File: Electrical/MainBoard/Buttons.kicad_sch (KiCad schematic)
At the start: 6 parts, among them SW10 User_Button, SW8 User_Button, SW9 User_Button

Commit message: Begin layout of pcb
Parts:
- renumbered SW9 to SW4, SW10 to SW5, SW8 to SW6
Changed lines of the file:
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@@
   (symbol (lib_id "power:+3.3V") (at 292.735 247.65 0) (unit 1)
     (in_bom yes) (on_board yes) (dnp no) (fields_autoplaced)
-    (property "Reference" "#PWR091" (at 292.735 251.46 0)
+    (property "Reference" "#PWR095" (at 292.735 251.46 0)
       (effects (font (size 1.27 1.27)) hide)
     )
@@
       (project "MainBoard"
         (path "/bd24c4db-4e36-4117-bd4f-5228ef241da9/41ea0116-63b8-412b-88a7-1e6a491b97c5"
-          (reference "#PWR091") (unit 1)
+          (reference "#PWR095") (unit 1)
         )
       )
@@
         )
         (path "/bd24c4db-4e36-4117-bd4f-5228ef241da9/41ea0116-63b8-412b-88a7-1e6a491b97c5"
-          (reference "R16") (unit 1)
+          (reference "R13") (unit 1)
         )
       )
@@
   (symbol (lib_id "power:+3.3V") (at 173.355 120.65 0) (unit 1)
     (in_bom yes) (on_board yes) (dnp no) (fields_autoplaced)
-    (property "Reference" "#PWR088" (at 173.355 124.46 0)
+    (property "Reference" "#PWR089" (at 173.355 124.46 0)
       (effects (font (size 1.27 1.27)) hide)
     )
@@
       (project "MainBoard"
         (path "/bd24c4db-4e36-4117-bd4f-5228ef241da9/41ea0116-63b8-412b-88a7-1e6a491b97c5"
-          (reference "#PWR088") (unit 1)
+          (reference "#PWR089") (unit 1)
         )
       )
@@
   (symbol (lib_id "Switch:SW_Push") (at 184.15 121.92 0) (unit 1)
     (in_bom yes) (on_board yes) (dnp no) (fields_autoplaced)
-    (property "Reference" "SW9" (at 184.15 114.3 0)
+    (property "Reference" "SW4" (at 184.15 114.3 0)
       (effects (font (size 1.27 1.27)))
     )
@@
       (project "MainBoard"
         (path "/bd24c4db-4e36-4117-bd4f-5228ef241da9/41ea0116-63b8-412b-88a7-1e6a491b97c5"
-          (reference "SW9") (unit 1)
+          (reference "SW4") (unit 1)
         )
       )
@@
   (symbol (lib_id "power:GND") (at 292.735 254.635 0) (unit 1)
     (in_bom yes) (on_board yes) (dnp no) (fields_autoplaced)
-    (property "Reference" "#PWR090" (at 292.735 260.985 0)
+    (property "Reference" "#PWR096" (at 292.735 260.985 0)
       (effects (font (size 1.27 1.27)) hide)
     )
@@
       (project "MainBoard"
         (path "/bd24c4db-4e36-4117-bd4f-5228ef241da9/41ea0116-63b8-412b-88a7-1e6a491b97c5"
-          (reference "#PWR090") (unit 1)
+          (reference "#PWR096") (unit 1)
         )
       )
@@
   (symbol (lib_id "power:GND") (at 192.405 129.54 0) (unit 1)
     (in_bom yes) (on_board yes) (dnp no) (fields_autoplaced)
-    (property "Reference" "#PWR085" (at 192.405 135.89 0)
+    (property "Reference" "#PWR092" (at 192.405 135.89 0)
       (effects (font (size 1.27 1.27)) hide)
     )
@@
       (project "MainBoard"
         (path "/bd24c4db-4e36-4117-bd4f-5228ef241da9/41ea0116-63b8-412b-88a7-1e6a491b97c5"
-          (reference "#PWR085") (unit 1)
+          (reference "#PWR092") (unit 1)
         )
       )
@@
   (symbol (lib_id "Switch:SW_Push") (at 184.785 100.33 0) (unit 1)
     (in_bom yes) (on_board yes) (dnp no) (fields_autoplaced)
-    (property "Reference" "SW8" (at 184.785 92.71 0)
+    (property "Reference" "SW6" (at 184.785 92.71 0)
       (effects (font (size 1.27 1.27)))
     )
@@
       (project "MainBoard"
         (path "/bd24c4db-4e36-4117-bd4f-5228ef241da9/41ea0116-63b8-412b-88a7-1e6a491b97c5"
-          (reference "SW8") (unit 1)
+          (reference "SW6") (unit 1)
         )
       )
@@
   (symbol (lib_id "power:+3.3V") (at 173.99 99.06 0) (unit 1)
     (in_bom yes) (on_board yes) (dnp no) (fields_autoplaced)
-    (property "Reference" "#PWR087" (at 173.99 102.87 0)
+    (property "Reference" "#PWR091" (at 173.99 102.87 0)
       (effects (font (size 1.27 1.27)) hide)
     )
@@
       (project "MainBoard"
         (path "/bd24c4db-4e36-4117-bd4f-5228ef241da9/41ea0116-63b8-412b-88a7-1e6a491b97c5"
-          (reference "#PWR087") (unit 1)
+          (reference "#PWR091") (unit 1)
         )
       )
@@
   (symbol (lib_id "power:GND") (at 192.405 147.955 0) (unit 1)
     (in_bom yes) (on_board yes) (dnp no) (fields_autoplaced)
-    (property "Reference" "#PWR086" (at 192.405 154.305 0)
+    (property "Reference" "#PWR093" (at 192.405 154.305 0)
       (effects (font (size 1.27 1.27)) hide)
     )
@@
       (project "MainBoard"
         (path "/bd24c4db-4e36-4117-bd4f-5228ef241da9/41ea0116-63b8-412b-88a7-1e6a491b97c5"
-          (reference "#PWR086") (unit 1)
+          (reference "#PWR093") (unit 1)
         )
       )
@@
   (symbol (lib_id "Switch:SW_Push") (at 184.15 140.335 0) (unit 1)
     (in_bom yes) (on_board yes) (dnp no) (fields_autoplaced)
-    (property "Reference" "SW10" (at 184.15 132.715 0)
+    (property "Reference" "SW5" (at 184.15 132.715 0)
       (effects (font (size 1.27 1.27)))
     )
@@
       (project "MainBoard"
         (path "/bd24c4db-4e36-4117-bd4f-5228ef241da9/41ea0116-63b8-412b-88a7-1e6a491b97c5"
-          (reference "SW10") (unit 1)
+          (reference "SW5") (unit 1)
         )
       )
@@
         )
         (path "/bd24c4db-4e36-4117-bd4f-5228ef241da9/41ea0116-63b8-412b-88a7-1e6a491b97c5"
-          (reference "R15") (unit 1)
+          (reference "R12") (unit 1)
         )
       )
@@
   (symbol (lib_id "power:+3.3V") (at 173.355 139.065 0) (unit 1)
     (in_bom yes) (on_board yes) (dnp no) (fields_autoplaced)
-    (property "Reference" "#PWR089" (at 173.355 142.875 0)
+    (property "Reference" "#PWR090" (at 173.355 142.875 0)
       (effects (font (size 1.27 1.27)) hide)
     )
@@
       (project "MainBoard"
         (path "/bd24c4db-4e36-4117-bd4f-5228ef241da9/41ea0116-63b8-412b-88a7-1e6a491b97c5"
-          (reference "#PWR089") (unit 1)
+          (reference "#PWR090") (unit 1)
         )
       )
@@
   (symbol (lib_id "power:GND") (at 193.04 107.95 0) (unit 1)
     (in_bom yes) (on_board yes) (dnp no) (fields_autoplaced)
-    (property "Reference" "#PWR084" (at 193.04 114.3 0)
+    (property "Reference" "#PWR094" (at 193.04 114.3 0)
       (effects (font (size 1.27 1.27)) hide)
     )
@@
       (project "MainBoard"
         (path "/bd24c4db-4e36-4117-bd4f-5228ef241da9/41ea0116-63b8-412b-88a7-1e6a491b97c5"
-          (reference "#PWR084") (unit 1)
-        )
-      )
+          (reference "#PWR094") (unit 1)
+        )
+      )

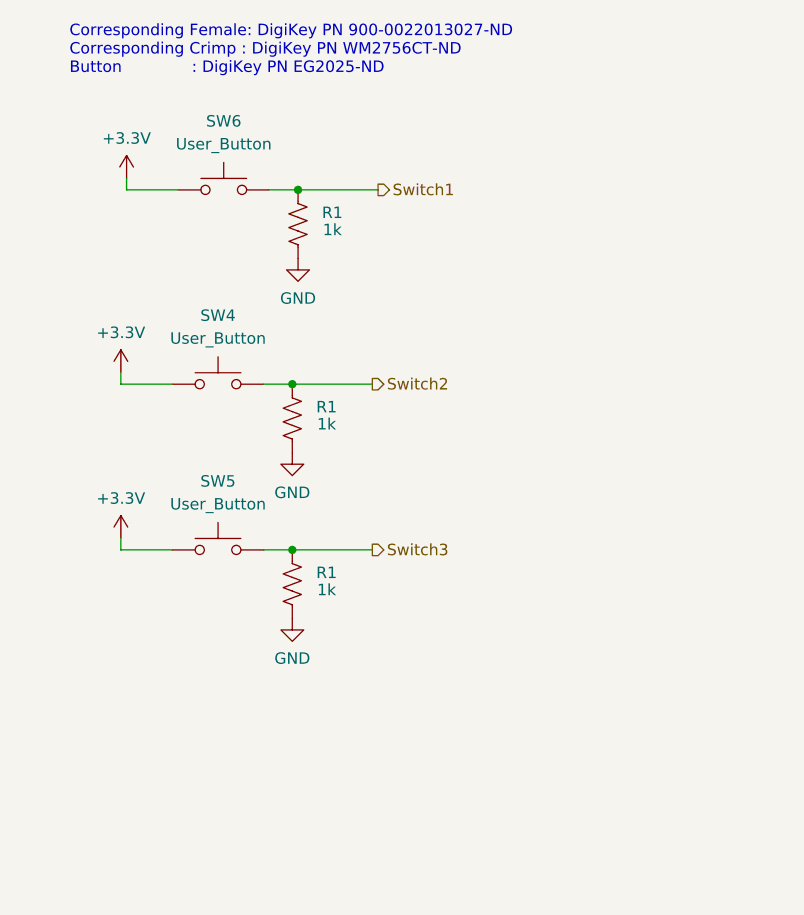
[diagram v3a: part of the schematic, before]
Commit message: Fix SPI3 and make visual improvements
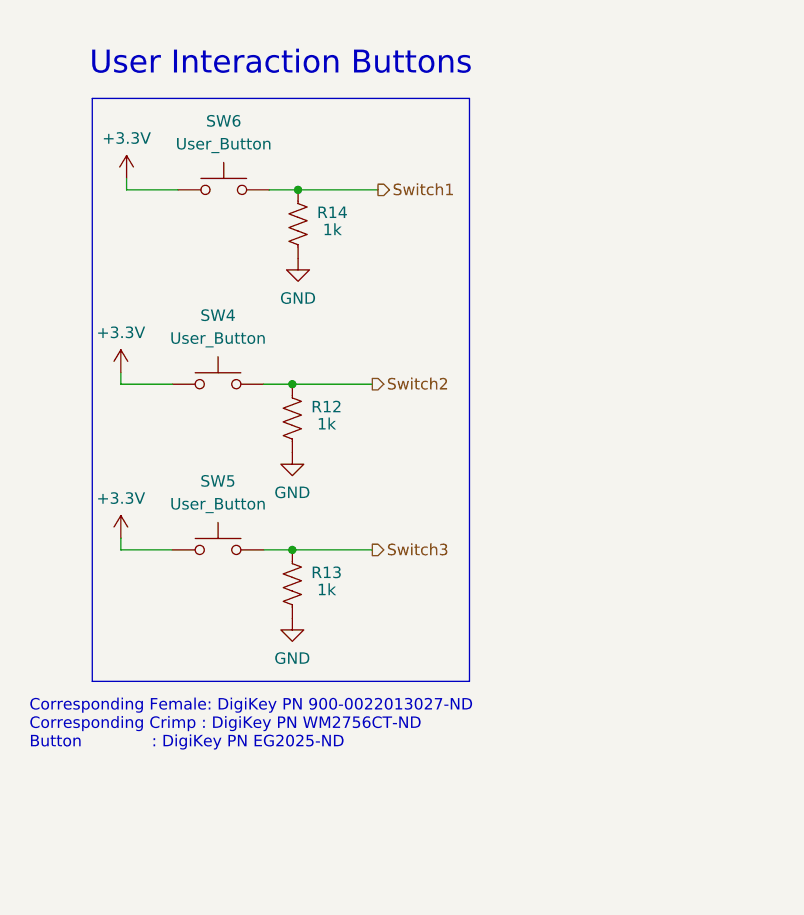
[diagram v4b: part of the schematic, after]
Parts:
- renumbered R1 to R12, R1 to R13, R1 to R14
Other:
- note added: "User Interaction Buttons"
